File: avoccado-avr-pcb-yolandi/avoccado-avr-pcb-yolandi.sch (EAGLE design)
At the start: 48 parts, among them Q1 16MHz, Q2 FET, U2 MCP73831

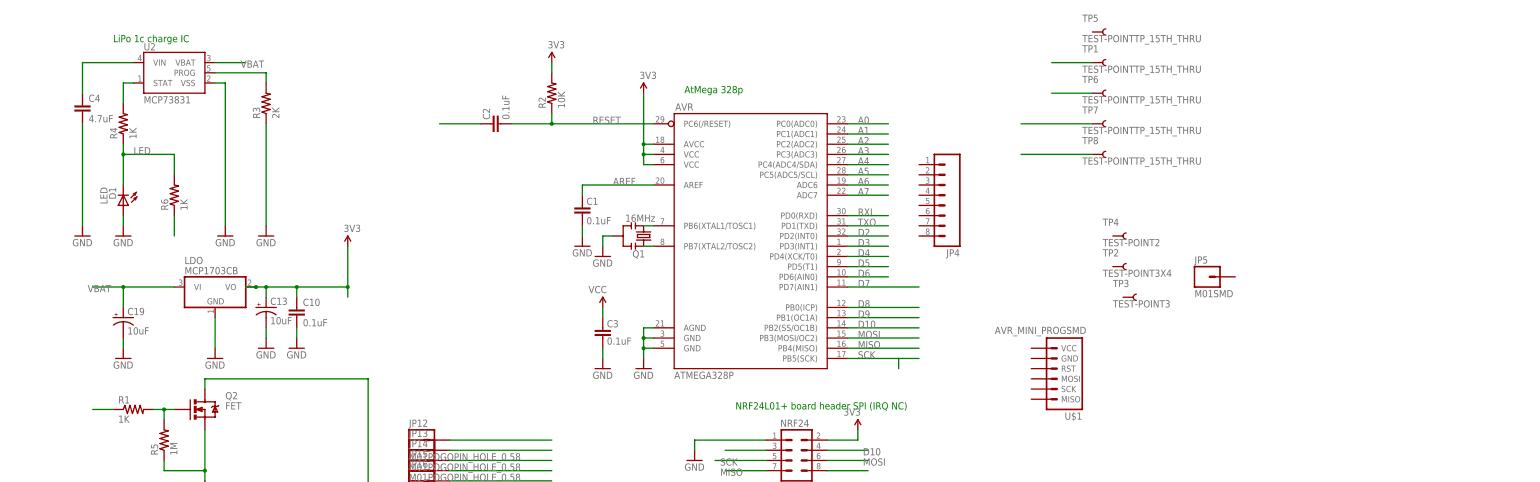
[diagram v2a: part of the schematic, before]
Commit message: routing yolandi, lower part with PDU
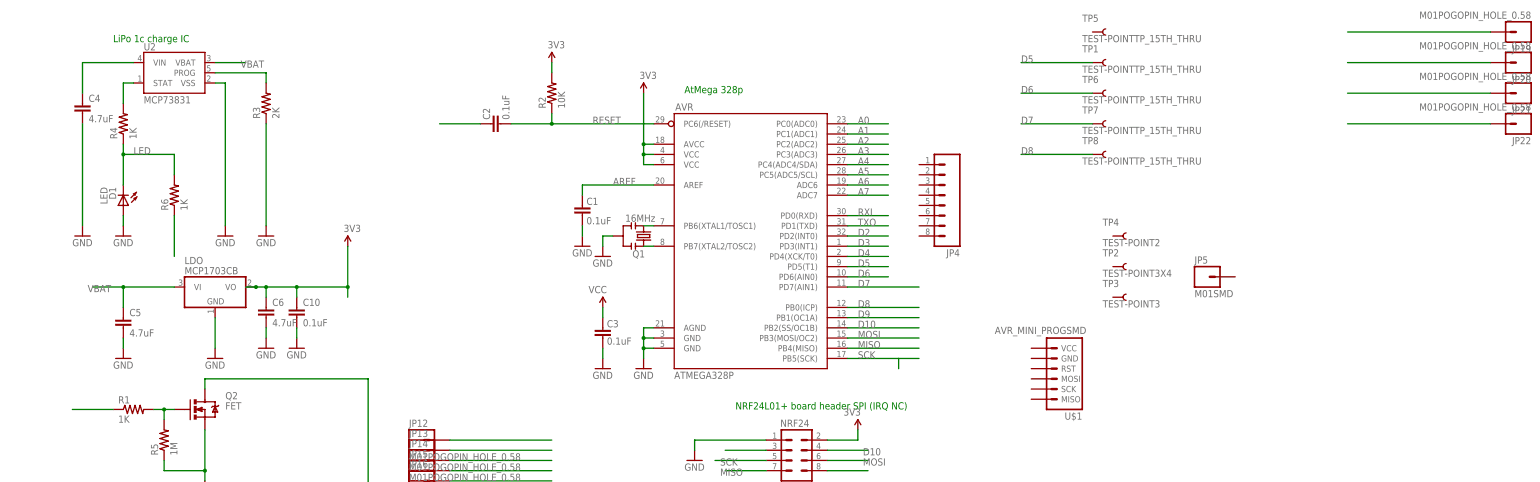
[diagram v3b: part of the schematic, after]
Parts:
- removed C13, C19: 10uF, SparkFun:CAP_POL1206
- added C5, C6: 4.7uF, SparkFun-Capacitors:4.7UF-6.3V-10%(0603)0603
- added JP19, JP20, JP21, JP22: M01POGOPIN_HOLE_0.58, SparkFun-Connectors:M01POGOPIN_HOLE_0.58
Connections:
- net 3V3: now also C6.1; no longer C13.+
- net A0: now also JP19.1
- net A1: now also JP20.1
- net A2: now also JP21.1
- net A3: now also JP22.1
- net D3: now also R6.1; no longer R1.1
- net D4: now also R1.1; no longer R6.1
- net GND: now also C5.2, C6.2; no longer C13.-, C19.-
- net VBAT: now also C5.1; no longer C19.+
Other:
- moved on the sheet: TP3
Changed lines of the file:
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@@
 <part name="C10" library="SparkFun" deviceset="CAP" device="0402" value="0.1uF"/>
 <part name="FRAME1" library="SparkFun" deviceset="FRAME-LETTER" device=""/>
-<part name="C13" library="SparkFun" deviceset="CAP_POL" device="1206" value="10uF"/>
 <part name="GND25" library="SparkFun" deviceset="GND" device=""/>
 <part name="GND26" library="SparkFun" deviceset="GND" device=""/>
@@
 <part name="C1" library="SparkFun" deviceset="CAP" device="0402" value="0.1uF"/>
 <part name="GND7" library="SparkFun" deviceset="GND" device=""/>
-<part name="C19" library="SparkFun" deviceset="CAP_POL" device="1206" value="10uF"/>
 <part name="GND30" library="SparkFun" deviceset="GND" device=""/>
 <part name="GND32" library="SparkFun" deviceset="GND" device=""/>
@@
 <part name="TP7" library="SparkFun-Passives" deviceset="TEST-POINT" device="TP_15TH_THRU"/>
 <part name="TP8" library="SparkFun-Passives" deviceset="TEST-POINT" device="TP_15TH_THRU"/>
+<part name="JP19" library="SparkFun-Connectors" deviceset="M01" device="POGOPIN_HOLE_0.58"/>
+<part name="JP20" library="SparkFun-Connectors" deviceset="M01" device="POGOPIN_HOLE_0.58"/>
+<part name="JP21" library="SparkFun-Connectors" deviceset="M01" device="POGOPIN_HOLE_0.58"/>
+<part name="JP22" library="SparkFun-Connectors" deviceset="M01" device="POGOPIN_HOLE_0.58"/>
+<part name="C5" library="SparkFun-Capacitors" deviceset="4.7UF-6.3V-10%(0603)" device="0603" value="4.7uF"/>
+<part name="C6" library="SparkFun-Capacitors" deviceset="4.7UF-6.3V-10%(0603)" device="0603" value="4.7uF"/>
 </parts>
 <sheets>
@@
 <instance part="FRAME1" gate="G$1" x="0" y="0"/>
 <instance part="FRAME1" gate="G$2" x="147.32" y="0"/>
-<instance part="C13" gate="G$1" x="71.12" y="109.22"/>
 <instance part="GND25" gate="1" x="71.12" y="99.06"/>
 <instance part="GND26" gate="1" x="78.74" y="99.06"/>
@@
 </instance>
 <instance part="GND7" gate="1" x="149.86" y="124.46"/>
-<instance part="C19" gate="G$1" x="35.56" y="106.68"/>
 <instance part="GND30" gate="1" x="58.42" y="96.52"/>
 <instance part="GND32" gate="1" x="35.56" y="96.52"/>
@@
 <instance part="JP4" gate="G$1" x="238.76" y="137.16" rot="R180"/>
 <instance part="TP2" gate="G$1" x="281.94" y="119.38"/>
-<instance part="TP3" gate="G$1" x="284.48" y="111.76"/>
+<instance part="TP3" gate="G$1" x="281.94" y="111.76"/>
 <instance part="TP4" gate="G$1" x="281.94" y="127"/>
 <instance part="TP5" gate="G$1" x="276.86" y="177.8"/>
@@
 <instance part="TP7" gate="G$1" x="276.86" y="154.94"/>
 <instance part="TP8" gate="G$1" x="276.86" y="147.32"/>
+<instance part="JP19" gate="G$1" x="383.54" y="177.8" rot="R180"/>
+<instance part="JP20" gate="G$1" x="383.54" y="170.18" rot="R180"/>
+<instance part="JP21" gate="G$1" x="383.54" y="162.56" rot="R180"/>
+<instance part="JP22" gate="G$1" x="383.54" y="154.94" rot="R180"/>
+<instance part="C5" gate="G$1" x="35.56" y="104.14"/>
+<instance part="C6" gate="G$1" x="71.12" y="106.68"/>
 </instances>
 <busses>
@@
 <segment>
 <wire x1="71.12" y1="101.6" x2="71.12" y2="104.14" width="0.1524" layer="91"/>
-<pinref part="C13" gate="G$1" pin="-"/>
 <pinref part="GND25" gate="1" pin="GND"/>
+<pinref part="C6" gate="G$1" pin="2"/>
 </segment>
 <segment>
@@
 <segment>
 <wire x1="35.56" y1="99.06" x2="35.56" y2="101.6" width="0.1524" layer="91"/>
-<pinref part="C19" gate="G$1" pin="-"/>
 <pinref part="GND32" gate="1" pin="GND"/>
+<pinref part="C5" gate="G$1" pin="2"/>
 </segment>
 <segment>
@@
 <pinref part="P+12" gate="G$1" pin="3.3V"/>
 <pinref part="C10" gate="G$1" pin="1"/>
-<pinref part="C13" gate="G$1" pin="+"/>
 <pinref part="LDO" gate="G$1" pin="VO"/>
 <junction x="68.58" y="114.3"/>
+<pinref part="C6" gate="G$1" pin="1"/>
 </segment>
 <segment>
@@
 <wire x1="259.08" y1="147.32" x2="276.86" y2="147.32" width="0.1524" layer="91"/>
 <pinref part="TP8" gate="G$1" pin="1"/>
+<label x="259.08" y="147.32" size="1.778" layer="95"/>
 </segment>
 </net>
@@
 <pinref part="AVR" gate="G$1" pin="PC3(ADC3)"/>
 </segment>
+<segment>
+<wire x1="340.36" y1="154.94" x2="375.92" y2="154.94" width="0.1524" layer="91"/>
+<pinref part="JP22" gate="G$1" pin="1"/>
+</segment>
 </net>
 <net name="A2" class="0">
@@
 <pinref part="AVR" gate="G$1" pin="PC2(ADC2)"/>
 </segment>
+<segment>
+<wire x1="340.36" y1="162.56" x2="375.92" y2="162.56" width="0.1524" layer="91"/>
+<pinref part="JP21" gate="G$1" pin="1"/>
+</segment>
 </net>
 <net name="A1" class="0">
@@
 <pinref part="AVR" gate="G$1" pin="PC1(ADC1)"/>
 </segment>
+<segment>
+<wire x1="340.36" y1="170.18" x2="375.92" y2="170.18" width="0.1524" layer="91"/>
+<pinref part="JP20" gate="G$1" pin="1"/>
+</segment>
 </net>
 <net name="A0" class="0">
@@
 <pinref part="AVR" gate="G$1" pin="PC0(ADC0)"/>
 </segment>
+<segment>
+<wire x1="340.36" y1="177.8" x2="375.92" y2="177.8" width="0.1524" layer="91"/>
+<pinref part="JP19" gate="G$1" pin="1"/>
+</segment>
 </net>
 <net name="D2" class="0">
@@
 </segment>
 <segment>
-<pinref part="R1" gate="G$1" pin="1"/>
-<wire x1="33.02" y1="83.82" x2="27.94" y2="83.82" width="0.1524" layer="91"/>
+<wire x1="48.26" y1="121.92" x2="48.26" y2="132.08" width="0.1524" layer="91"/>
+<pinref part="R6" gate="G$1" pin="1"/>
 </segment>
 </net>
@@
 </segment>
 <segment>
-<pinref part="R6" gate="G$1" pin="1"/>
-<wire x1="48.26" y1="132.08" x2="48.26" y2="127" width="0.1524" layer="91"/>
+<wire x1="22.86" y1="83.82" x2="33.02" y2="83.82" width="0.1524" layer="91"/>
+<pinref part="R1" gate="G$1" pin="1"/>
 </segment>
 </net>
@@
 </segment>
 <segment>
-<wire x1="266.7" y1="170.18" x2="276.86" y2="170.18" width="0.1524" layer="91"/>
+<wire x1="259.08" y1="170.18" x2="276.86" y2="170.18" width="0.1524" layer="91"/>
 <pinref part="TP1" gate="G$1" pin="1"/>
+<label x="259.08" y="170.18" size="1.778" layer="95"/>
 </segment>
 </net>
@@
 </segment>
 <segment>
-<wire x1="266.7" y1="162.56" x2="276.86" y2="162.56" width="0.1524" layer="91"/>
+<wire x1="259.08" y1="162.56" x2="276.86" y2="162.56" width="0.1524" layer="91"/>
 <pinref part="TP6" gate="G$1" pin="1"/>
+<label x="259.08" y="162.56" size="1.778" layer="95"/>
 </segment>
 </net>
@@
 <wire x1="259.08" y1="154.94" x2="276.86" y2="154.94" width="0.1524" layer="91"/>
 <pinref part="TP7" gate="G$1" pin="1"/>
+<label x="259.08" y="154.94" size="1.778" layer="95"/>
 </segment>
 </net>
@@
 <junction x="35.56" y="114.3"/>
 <label x="26.67" y="113.03" size="1.778" layer="95"/>
-<pinref part="C19" gate="G$1" pin="+"/>
 <pinref part="LDO" gate="G$1" pin="VI"/>
 <label x="64.77" y="168.91" size="1.778" layer="95"/>
-</segment>
-<segment>
+<pinref part="C5" gate="G$1" pin="1"/>
+</segment>
+<segment>

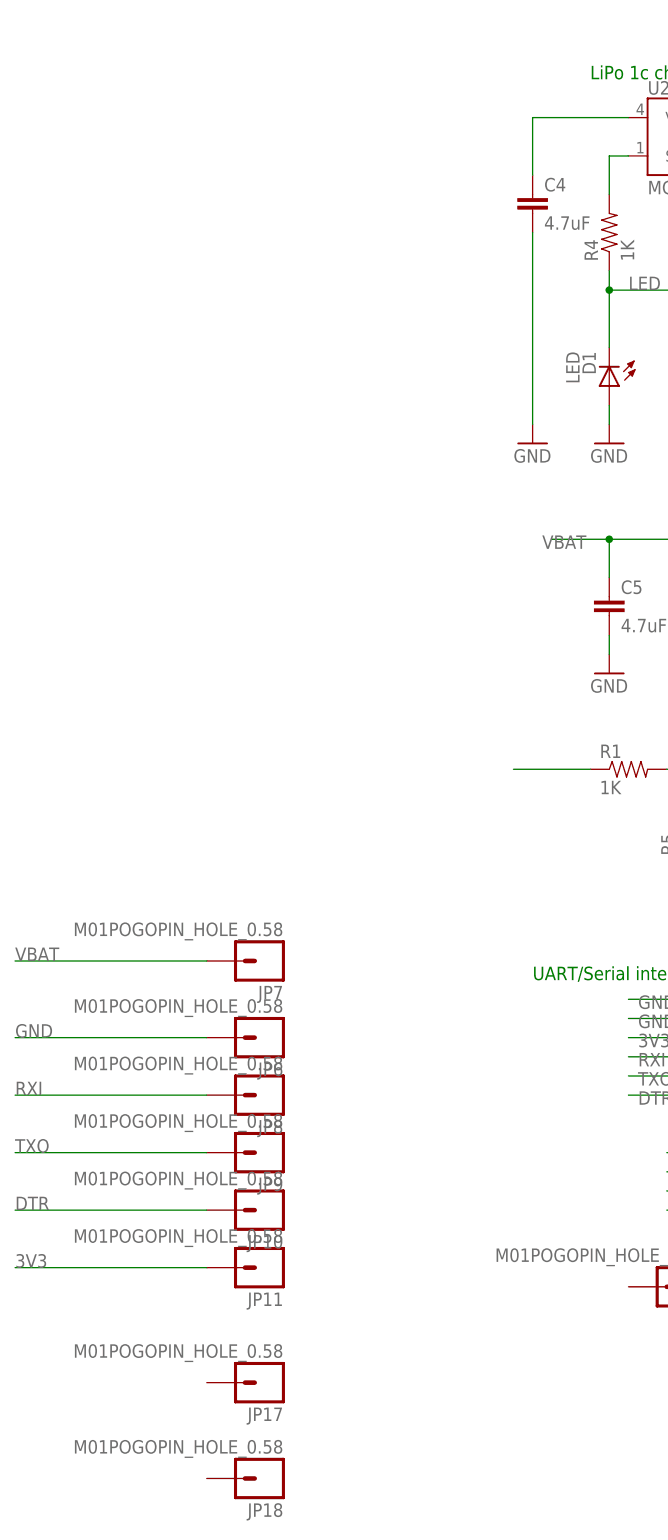
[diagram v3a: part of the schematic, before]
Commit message: routing the buffered load output
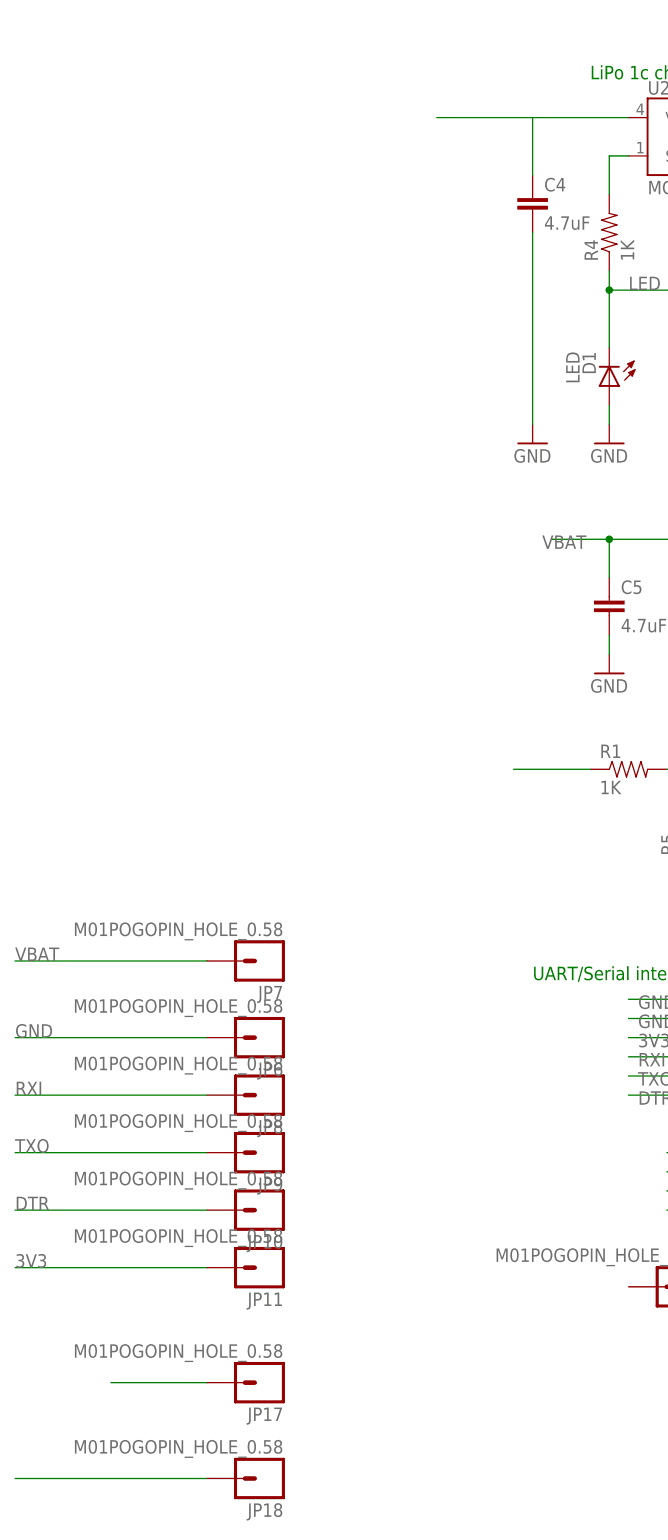
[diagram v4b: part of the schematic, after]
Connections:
- net 3V3: now also JP18.1
- net 5V: now also JP17.1
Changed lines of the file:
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@@
 <label x="-43.18" y="17.78" size="1.778" layer="95"/>
+</segment>
+<segment>
+<wire x1="-43.18" y1="-10.16" x2="-17.78" y2="-10.16" width="0.1524" layer="91"/>
+<pinref part="JP18" gate="G$1" pin="1"/>
 </segment>
 </net>
@@
 <pinref part="C4" gate="G$1" pin="1"/>
 <wire x1="25.4" y1="170.18" x2="25.4" y2="162.56" width="0.1524" layer="91"/>
-</segment>
-</net>
+<wire x1="12.7" y1="170.18" x2="25.4" y2="170.18" width="0.1524" layer="91"/>
+</segment>
+<segment>
+<wire x1="-30.48" y1="2.54" x2="-17.78" y2="2.54" width="0.1524" layer="91"/>
+<pinref part="JP17" gate="G$1" pin="1"/>
+</segment>
+</net>

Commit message: wip yolandi
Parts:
- added JP24: M01POGOPIN_HOLE_0.58, SparkFun-Connectors:M01POGOPIN_HOLE_0.58
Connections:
- net GND: now also JP3.1
- net VBAT: now also JP24.1
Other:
- moved on the sheet: JP3
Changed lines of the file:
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@@
 <part name="C5" library="SparkFun-Capacitors" deviceset="4.7UF-6.3V-10%(0603)" device="0603" value="4.7uF"/>
 <part name="C6" library="SparkFun-Capacitors" deviceset="4.7UF-6.3V-10%(0603)" device="0603" value="4.7uF"/>
+<part name="JP24" library="SparkFun-Connectors" deviceset="M01" device="POGOPIN_HOLE_0.58"/>
 </parts>
 <sheets>
@@
 <instance part="JP15" gate="G$1" x="109.22" y="68.58"/>
 <instance part="JP16" gate="G$1" x="109.22" y="66.04"/>
-<instance part="JP3" gate="G$1" x="45.72" y="15.24" rot="R180"/>
+<instance part="JP3" gate="G$1" x="-10.16" y="86.36" rot="R180"/>
 <instance part="JP17" gate="G$1" x="-10.16" y="2.54" rot="R180"/>
 <instance part="JP18" gate="G$1" x="-10.16" y="-10.16" rot="R180"/>
@@
 <instance part="C5" gate="G$1" x="35.56" y="104.14"/>
 <instance part="C6" gate="G$1" x="71.12" y="106.68"/>
+<instance part="JP24" gate="G$1" x="-10.16" y="-35.56" rot="R180"/>
 </instances>
 <busses>
@@
 <pinref part="JP6" gate="G$1" pin="1"/>
 <label x="-43.18" y="48.26" size="1.778" layer="95"/>
+<label x="-43.18" y="86.36" size="1.778" layer="95"/>
+</segment>
+<segment>
+<wire x1="-17.78" y1="86.36" x2="-43.18" y2="86.36" width="0.1524" layer="91"/>
+<pinref part="JP3" gate="G$1" pin="1"/>
 </segment>
 </net>
@@
 <wire x1="-43.18" y1="-10.16" x2="-17.78" y2="-10.16" width="0.1524" layer="91"/>
 <pinref part="JP18" gate="G$1" pin="1"/>
+<label x="-43.18" y="-10.16" size="1.778" layer="95"/>
 </segment>
 </net>
@@
 </segment>
 <segment>
-<wire x1="-30.48" y1="2.54" x2="-17.78" y2="2.54" width="0.1524" layer="91"/>
+<wire x1="-43.18" y1="2.54" x2="-17.78" y2="2.54" width="0.1524" layer="91"/>
 <pinref part="JP17" gate="G$1" pin="1"/>
+<label x="-43.18" y="2.54" size="1.778" layer="95"/>
 </segment>
 </net>
@@
 <label x="-43.18" y="58.42" size="1.778" layer="95"/>
 </segment>
-</net>
+<segment>
+<wire x1="-17.78" y1="-35.56" x2="-43.18" y2="-35.56" width="0.1524" layer="91"/>
+<pinref part="JP24" gate="G$1" pin="1"/>
+<label x="-43.18" y="-35.56" size="1.778" layer="95"/>
+</segment>
+</net>

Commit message: wip add silkscreen
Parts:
- removed JP2: (no value), SparkFun-Connectors:M08NO_SILK
- added JP23, JP25, JP26: M01POGOPIN_HOLE_0.58, SparkFun-Connectors:M01POGOPIN_HOLE_0.58
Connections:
- net GND: now also D1.C, JP25.1, JP26.1; no longer D1.A
- net LED: now also D1.A; no longer D1.C
- net VIBR: now also JP23.1
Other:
- moved on the sheet: D1
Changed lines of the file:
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@@
 <part name="JP1" library="SparkFun-Connectors" deviceset="M08" device="NO_SILK"/>
 <part name="R6" library="SparkFun-Resistors" deviceset="RESISTOR" device="0603" value="1K"/>
-<part name="JP2" library="SparkFun-Connectors" deviceset="M08" device="NO_SILK"/>
 <part name="JP4" library="SparkFun-Connectors" deviceset="M08" device="NO_SILK"/>
 <part name="TP2" library="SparkFun-Passives" deviceset="TEST-POINT" device="3X4"/>
@@
 <part name="C6" library="SparkFun-Capacitors" deviceset="4.7UF-6.3V-10%(0603)" device="0603" value="4.7uF"/>
 <part name="JP24" library="SparkFun-Connectors" deviceset="M01" device="POGOPIN_HOLE_0.58"/>
+<part name="JP23" library="SparkFun-Connectors" deviceset="M01" device="POGOPIN_HOLE_0.58"/>
+<part name="JP25" library="SparkFun-Connectors" deviceset="M01" device="POGOPIN_HOLE_0.58"/>
+<part name="JP26" library="SparkFun-Connectors" deviceset="M01" device="POGOPIN_HOLE_0.58"/>
 </parts>
 <sheets>
@@
 <instance part="R3" gate="G$1" x="71.12" y="160.02" rot="R90"/>
 <instance part="GND3" gate="1" x="71.12" y="127"/>
-<instance part="D1" gate="G$1" x="35.56" y="134.62" rot="R180"/>
+<instance part="D1" gate="G$1" x="35.56" y="142.24" rot="MR0"/>
 <instance part="C4" gate="G$1" x="25.4" y="157.48"/>
 <instance part="R4" gate="G$1" x="35.56" y="154.94" rot="R90"/>
@@
 <instance part="JP1" gate="G$1" x="213.36" y="48.26" rot="R180"/>
 <instance part="R6" gate="G$1" x="48.26" y="137.16" rot="R90"/>
-<instance part="JP2" gate="G$1" x="241.3" y="48.26" rot="R180"/>
 <instance part="JP4" gate="G$1" x="238.76" y="137.16" rot="R180"/>
 <instance part="TP2" gate="G$1" x="281.94" y="119.38"/>
@@
 <instance part="C6" gate="G$1" x="71.12" y="106.68"/>
 <instance part="JP24" gate="G$1" x="-10.16" y="-35.56" rot="R180"/>
+<instance part="JP23" gate="G$1" x="-10.16" y="76.2" rot="R180"/>
+<instance part="JP25" gate="G$1" x="-10.16" y="-25.4" rot="R180"/>
+<instance part="JP26" gate="G$1" x="-10.16" y="-45.72" rot="R180"/>
 </instances>
 <busses>
@@
 </segment>
 <segment>
-<pinref part="GND6" gate="1" pin="GND"/>
-<wire x1="35.56" y1="129.54" x2="35.56" y2="132.08" width="0.1524" layer="91"/>
-<pinref part="D1" gate="G$1" pin="A"/>
-</segment>
-<segment>
 <wire x1="55.88" y1="43.18" x2="91.44" y2="43.18" width="0.1524" layer="91"/>
 </segment>
@@
 <wire x1="-17.78" y1="86.36" x2="-43.18" y2="86.36" width="0.1524" layer="91"/>
 <pinref part="JP3" gate="G$1" pin="1"/>
+</segment>
+<segment>
+<wire x1="-17.78" y1="-25.4" x2="-43.18" y2="-25.4" width="0.1524" layer="91"/>
+<pinref part="JP25" gate="G$1" pin="1"/>
+<label x="-43.18" y="-25.4" size="1.778" layer="95"/>
+</segment>
+<segment>
+<wire x1="-17.78" y1="-45.72" x2="-43.18" y2="-45.72" width="0.1524" layer="91"/>
+<pinref part="JP26" gate="G$1" pin="1"/>
+<label x="-43.18" y="-45.72" size="1.778" layer="95"/>
+</segment>
+<segment>
+<pinref part="D1" gate="G$1" pin="C"/>
+<pinref part="GND6" gate="1" pin="GND"/>
+<wire x1="35.56" y1="137.16" x2="35.56" y2="129.54" width="0.1524" layer="91"/>
 </segment>
 </net>
@@
 <wire x1="96.52" y1="48.26" x2="63.5" y2="48.26" width="0.2032" layer="91"/>
 </segment>
+<segment>
+<wire x1="-17.78" y1="76.2" x2="-43.18" y2="76.2" width="0.2032" layer="91"/>
+<pinref part="JP23" gate="G$1" pin="1"/>
+<label x="-43.18" y="76.2" size="1.778" layer="95"/>
+</segment>
 </net>
 <net name="VBAT" class="1">
@@
 <net name="LED" class="0">
 <segment>
-<pinref part="D1" gate="G$1" pin="C"/>
 <pinref part="R4" gate="G$1" pin="1"/>
-<wire x1="35.56" y1="139.7" x2="35.56" y2="147.32" width="0.1524" layer="91"/>
 <wire x1="35.56" y1="147.32" x2="35.56" y2="149.86" width="0.1524" layer="91"/>
 <wire x1="35.56" y1="147.32" x2="48.26" y2="147.32" width="0.1524" layer="91"/>
-<junction x="35.56" y="147.32"/>
 <label x="38.1" y="147.32" size="1.778" layer="95"/>
 <pinref part="R6" gate="G$1" pin="2"/>
 <wire x1="48.26" y1="147.32" x2="48.26" y2="142.24" width="0.1524" layer="91"/>
-</segment>
-</net>
+<pinref part="D1" gate="G$1" pin="A"/>
+<wire x1="35.56" y1="144.78" x2="35.56" y2="147.32" width="0.1524" layer="91"/>
+<junction x="35.56" y="147.32"/>
+</segment>
+</net>
